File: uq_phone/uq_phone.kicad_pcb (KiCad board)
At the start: 4 copper layers, 116.9 x 105 mm, 164 parts, among them J1 USB4105-GF-A, J10 SJ-3551B-MSMT-TR-67, J11 Conn_01x02, J2 S3B-PH-SM4-TB_LF__SN_, J3 20279-001E-03, J4 20279-001E-03, J6 Conn_ARM_SWD_TagConnect_TC2030, J7 Conn_01x02, J8 KP15B-6S-SF_800_, J9 541324562, M1 VCDM0834B004L, Q1 MMBT3904LP-7, Q2 MMBT3904LP-7, U1 MCP73871-2CCI_ML, U10 TPD3F303DQDR, U11 TPD8F003DQDR, U12 MCP1664T-E/OT, U13 TS3A5018RSVR, U14 NAU88C22YG, U2 TPS62162DSGR, U3 BQ27441DRZR-G1A, U4 RC7620_1104625, U5 TXB0108RGYR, U6 TXB0108RGYR, U7 STM32H730VBTx, U8 LSM6DSVTR, U9 DRV2603RUNR

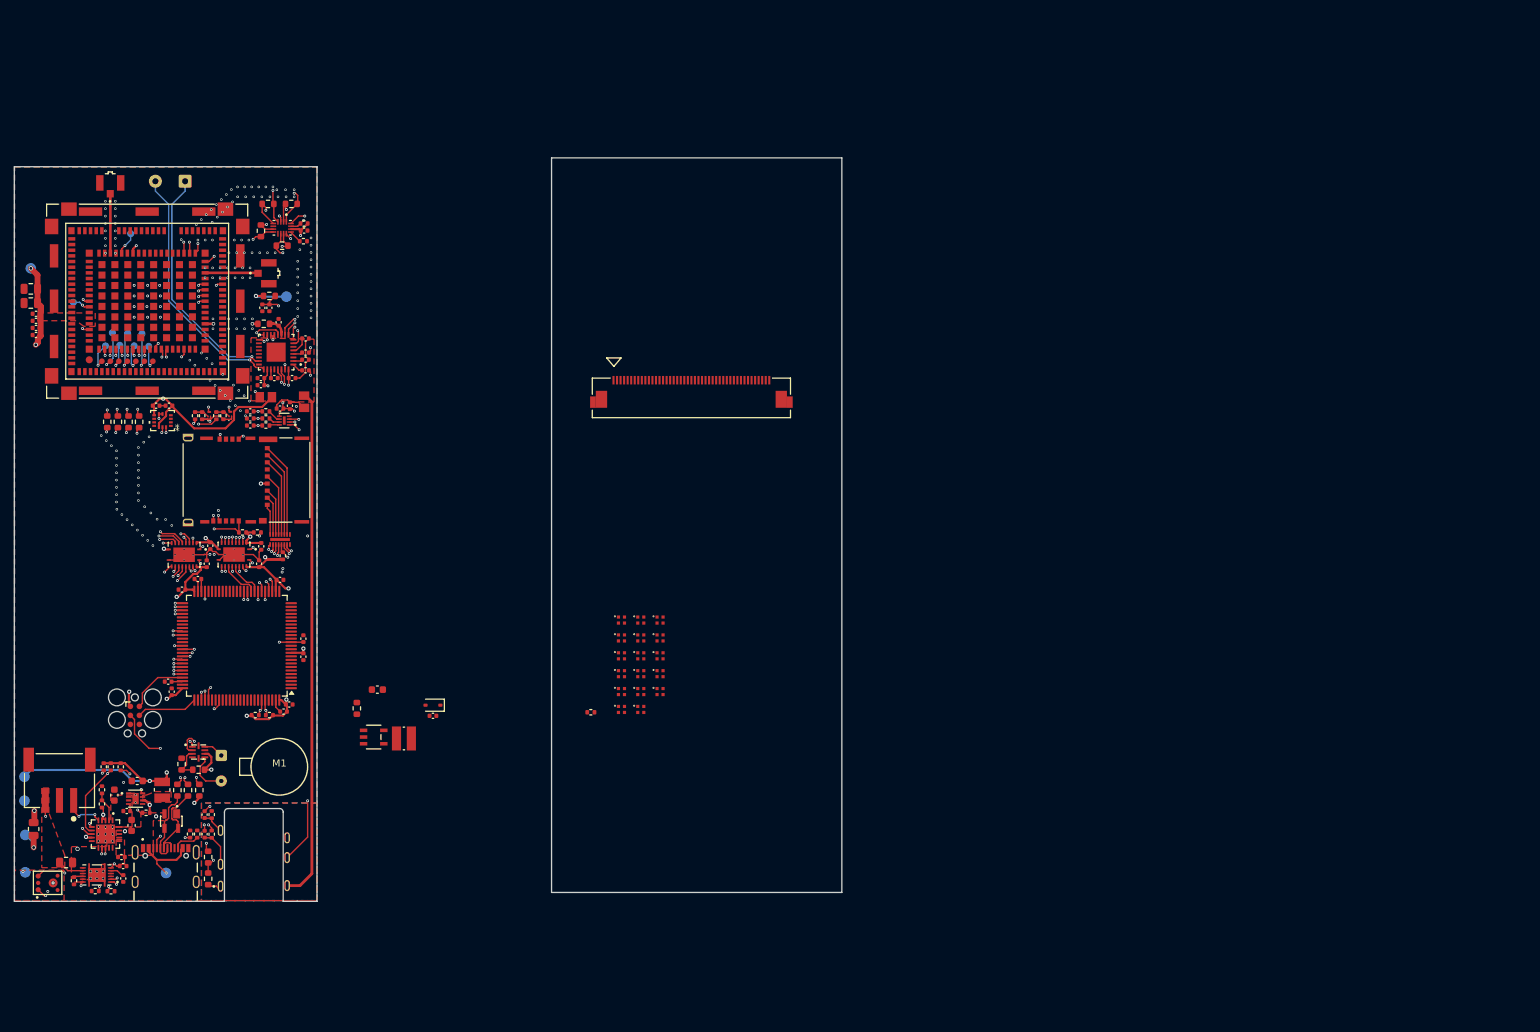
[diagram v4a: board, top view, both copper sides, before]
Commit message: Update pcb and remove Stm32 profile
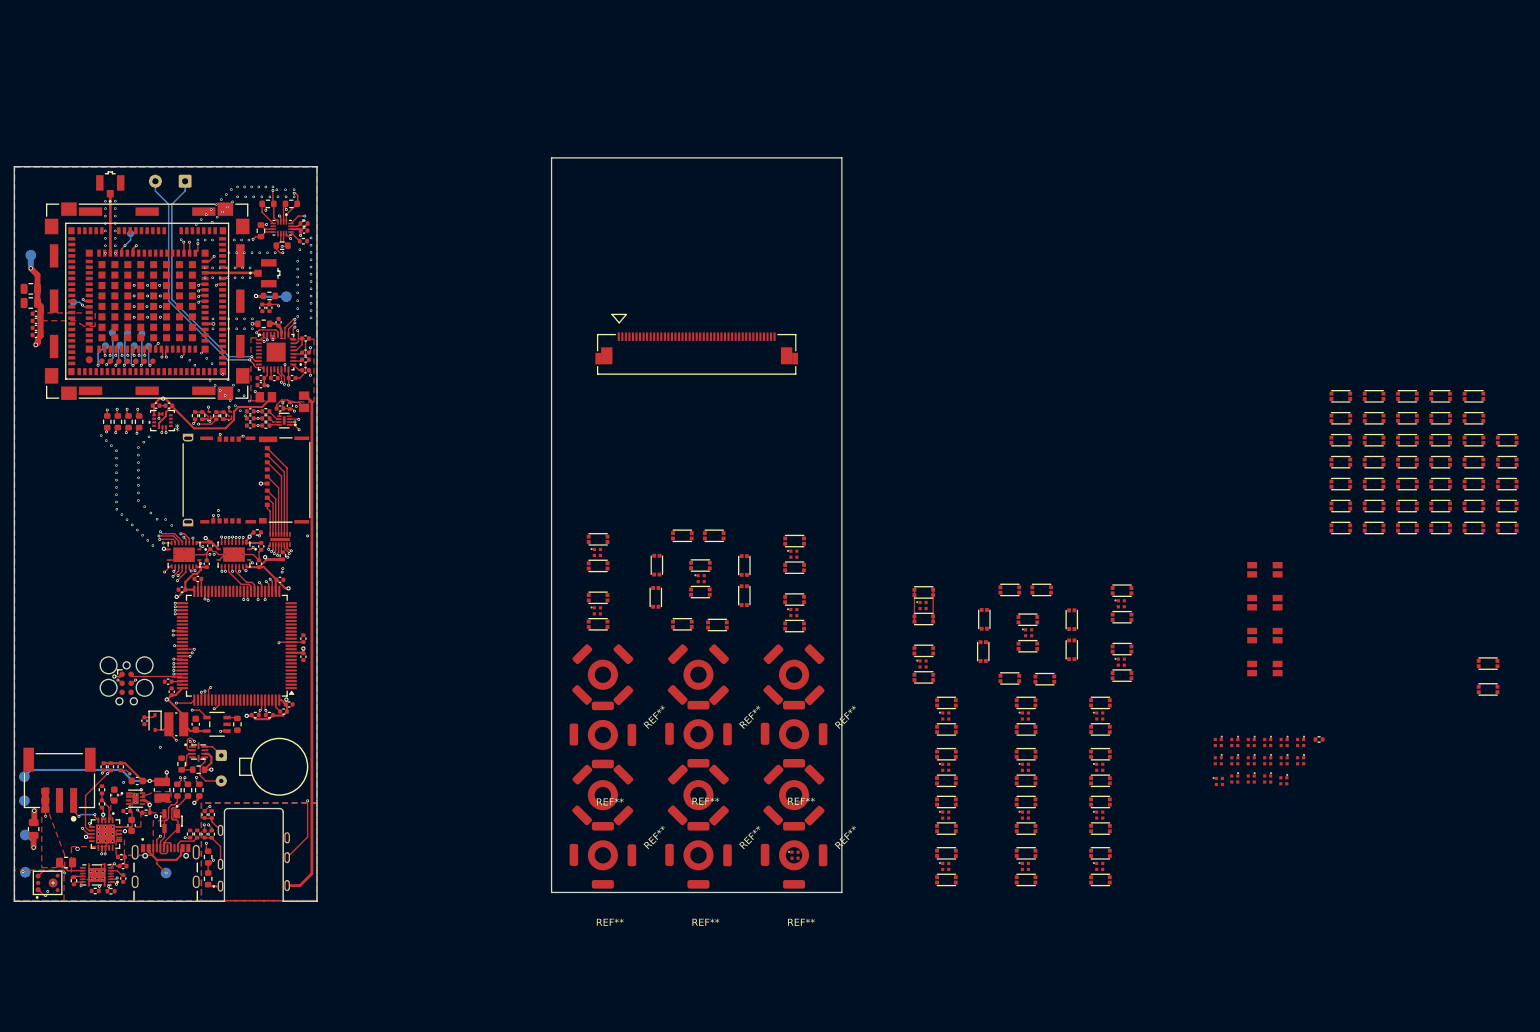
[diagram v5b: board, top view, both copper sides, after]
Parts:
- removed the LED13 at (118.2, 131.8)
- removed R23: 10k, Resistor_SMD:R_0402_1005Metric
- added LED13: XL-1010RGBC, custom_footprints:XL-1010RGBC-WS2812B, F.Cu at (137.1, 131.7)
- added LED13: XL-1010RGBC, custom_footprints:XL-1010RGBC-WS2812B, F.Cu at (169.8, 167.5)
- added LED13: XL-1010RGBC, custom_footprints:XL-1010RGBC-WS2812B, F.Cu at (180.2, 146.2)
- added LED13: XL-1010RGBC, custom_footprints:XL-1010RGBC-WS2812B, F.Cu at (137.1, 123.4)
- added LED13: XL-1010RGBC, custom_footprints:XL-1010RGBC-WS2812B, F.Cu at (155.3, 130.7)
- added LED13: XL-1010RGBC, custom_footprints:XL-1010RGBC-WS2812B, F.Cu at (158.5, 167.5)
- added LED13: XL-1010RGBC, custom_footprints:XL-1010RGBC-WS2812B, F.Cu at (180.2, 153.5)
- added LED13: XL-1010RGBC, custom_footprints:XL-1010RGBC-WS2812B, F.Cu at (124.0, 126.8)
- added LED13: XL-1010RGBC, custom_footprints:XL-1010RGBC-WS2812B, F.Cu at (180.2, 167.5)
- added LED13: XL-1010RGBC, custom_footprints:XL-1010RGBC-WS2812B, F.Cu at (170.2, 134.5)
- added LED13: XL-1010RGBC, custom_footprints:XL-1010RGBC-WS2812B, F.Cu at (183.3, 138.7)
- added LED13: XL-1010RGBC, custom_footprints:XL-1010RGBC-WS2812B, F.Cu at (158.5, 160.2)
- added LED13: XL-1010RGBC, custom_footprints:XL-1010RGBC-WS2812B, F.Cu at (137.2, 165.9)
- added LED13: XL-1010RGBC, custom_footprints:XL-1010RGBC-WS2812B, F.Cu at (109.3, 123.2)
- added LED13: XL-1010RGBC, custom_footprints:XL-1010RGBC-WS2812B, F.Cu at (197.2, 155.5)
- added LED13: XL-1010RGBC, custom_footprints:XL-1010RGBC-WS2812B, F.Cu at (155.3, 138.9)
- added LED13: XL-1010RGBC, custom_footprints:XL-1010RGBC-WS2812B, F.Cu at (169.8, 160.2)
- added LED13: XL-1010RGBC, custom_footprints:XL-1010RGBC-WS2812B, F.Cu at (183.3, 130.4)
- added LED13: XL-1010RGBC, custom_footprints:XL-1010RGBC-WS2812B, F.Cu at (169.8, 153.5)
- added LED13: XL-1010RGBC, custom_footprints:XL-1010RGBC-WS2812B, F.Cu at (158.5, 153.5)
- added LED13: XL-1010RGBC, custom_footprints:XL-1010RGBC-WS2812B, F.Cu at (169.8, 146.2)
- added LED13: XL-1010RGBC, custom_footprints:XL-1010RGBC-WS2812B, F.Cu at (109.3, 131.4)
- added LED13: XL-1010RGBC, custom_footprints:XL-1010RGBC-WS2812B, F.Cu at (180.2, 160.2)
- added LED13: XL-1010RGBC, custom_footprints:XL-1010RGBC-WS2812B, F.Cu at (158.5, 146.2)
- added REF**: 8.5mmSnaptron, custom_footprints:8.5mmSnaptron, F.Cu at (110.5, 157.0)
- added REF**: 8.5mmSnaptron, custom_footprints:8.5mmSnaptron, F.Cu at (124.0, 165.5)
- added REF**: 8.5mmSnaptron, custom_footprints:8.5mmSnaptron, F.Cu at (137.5, 140.0)
- added REF**: 8.5mmSnaptron, custom_footprints:8.5mmSnaptron, F.Cu at (137.5, 165.5)
- added REF**: 8.5mmSnaptron, custom_footprints:8.5mmSnaptron, F.Cu at (124.0, 157.0)
- added REF**: 8.5mmSnaptron, custom_footprints:8.5mmSnaptron, F.Cu at (110.5, 148.5)
- added REF**: 8.5mmSnaptron, custom_footprints:8.5mmSnaptron, F.Cu at (124.0, 148.4)
- added REF**: 8.5mmSnaptron, custom_footprints:8.5mmSnaptron, F.Cu at (124.0, 140.0)
- added REF**: 8.5mmSnaptron, custom_footprints:8.5mmSnaptron, F.Cu at (110.5, 140.0)
- added REF**: 8.5mmSnaptron, custom_footprints:8.5mmSnaptron, F.Cu at (137.5, 148.4)
- added REF**: 8.5mmSnaptron, custom_footprints:8.5mmSnaptron, F.Cu at (110.5, 165.5)
- added REF**: 8.5mmSnaptron, custom_footprints:8.5mmSnaptron, F.Cu at (137.5, 157.0)
- added SW1: SKTAAAE010, custom_footprints:SKTAAAE010, F.Cu at (213.4, 100.3)
- added SW10: SKTAAAE010, custom_footprints:SKTAAAE010, F.Cu at (218.1, 106.5)
- added SW11: SKTAAAE010, custom_footprints:SKTAAAE010, F.Cu at (218.1, 109.6)
- added SW12: SKTAAAE010, custom_footprints:SKTAAAE010, F.Cu at (218.1, 112.7)
- added SW13: SKTAAAE010, custom_footprints:SKTAAAE010, F.Cu at (218.1, 115.8)
- added SW14: SKTAAAE010, custom_footprints:SKTAAAE010, F.Cu at (218.1, 118.9)
- added SW15: SKTAAAE010, custom_footprints:SKTAAAE010, F.Cu at (222.8, 100.3)
- added SW16: SKTAAAE010, custom_footprints:SKTAAAE010, F.Cu at (222.8, 103.4)
- added SW17: SKTAAAE010, custom_footprints:SKTAAAE010, F.Cu at (222.8, 106.5)
- added SW18: SKTAAAE010, custom_footprints:SKTAAAE010, F.Cu at (222.8, 109.6)
- added SW19: SKTAAAE010, custom_footprints:SKTAAAE010, F.Cu at (222.8, 112.7)
- added SW2: SKTAAAE010, custom_footprints:SKTAAAE010, F.Cu at (213.4, 103.4)
- added SW20: SKTAAAE010, custom_footprints:SKTAAAE010, F.Cu at (222.8, 115.8)
- added SW21: SKTAAAE010, custom_footprints:SKTAAAE010, F.Cu at (222.8, 118.9)
- added SW22: SKTAAAE010, custom_footprints:SKTAAAE010, F.Cu at (227.5, 100.3)
- added SW23: SKTAAAE010, custom_footprints:SKTAAAE010, F.Cu at (227.5, 103.4)
- added SW24: SKTAAAE010, custom_footprints:SKTAAAE010, F.Cu at (227.5, 106.5)
- added SW25: SKTAAAE010, custom_footprints:SKTAAAE010, F.Cu at (227.5, 109.6)
- added SW26: SKTAAAE010, custom_footprints:SKTAAAE010, F.Cu at (227.5, 112.7)
- added SW27: SKTAAAE010, custom_footprints:SKTAAAE010, F.Cu at (227.5, 115.8)
- added SW28: SKTAAAE010, custom_footprints:SKTAAAE010, F.Cu at (227.5, 118.9)
- added SW29: SKTAAAE010, custom_footprints:SKTAAAE010, F.Cu at (232.2, 100.3)
- added SW3: SKTAAAE010, custom_footprints:SKTAAAE010, F.Cu at (213.4, 106.5)
- added SW30: SKTAAAE010, custom_footprints:SKTAAAE010, F.Cu at (232.2, 103.4)
- added SW31: SKTAAAE010, custom_footprints:SKTAAAE010, F.Cu at (232.2, 106.5)
- added SW32: SKTAAAE010, custom_footprints:SKTAAAE010, F.Cu at (232.2, 109.6)
- added SW33: SKTAAAE010, custom_footprints:SKTAAAE010, F.Cu at (232.2, 112.7)
- added SW34: SKTAAAE010, custom_footprints:SKTAAAE010, F.Cu at (232.2, 115.8)
- added SW35: SKTAAAE010, custom_footprints:SKTAAAE010, F.Cu at (232.2, 118.9)
- added SW36: SKTAAAE010, custom_footprints:SKTAAAE010, F.Cu at (174.2, 141.0)
- added SW36: SKTAAAE010, custom_footprints:SKTAAAE010, F.Cu at (136.2, 132.8)
- added SW36: SKTAAAE010, custom_footprints:SKTAAAE010, F.Cu at (169.3, 140.9)
- added SW36: SKTAAAE010, custom_footprints:SKTAAAE010, F.Cu at (179.4, 157.6)
- added SW36: SKTAAAE010, custom_footprints:SKTAAAE010, F.Cu at (136.2, 129.0)
- added SW36: SKTAAAE010, custom_footprints:SKTAAAE010, F.Cu at (136.2, 124.5)
- added SW36: SKTAAAE010, custom_footprints:SKTAAAE010, F.Cu at (108.5, 132.5)
- added SW36: SKTAAAE010, custom_footprints:SKTAAAE010, F.Cu at (128.0, 133.3)
- added SW36: SKTAAAE010, custom_footprints:SKTAAAE010, F.Cu at (179.4, 161.3)
- added SW36: SKTAAAE010, custom_footprints:SKTAAAE010, F.Cu at (179.4, 164.8)
- added SW36: SKTAAAE010, custom_footprints:SKTAAAE010, F.Cu at (176.3, 133.6)
- added SW36: SKTAAAE010, custom_footprints:SKTAAAE010, F.Cu at (164.0, 133.5)
- added SW36: SKTAAAE010, custom_footprints:SKTAAAE010, F.Cu at (123.0, 128.0)
- added SW36: SKTAAAE010, custom_footprints:SKTAAAE010, F.Cu at (169.2, 135.6)
- added SW36: SKTAAAE010, custom_footprints:SKTAAAE010, F.Cu at (108.5, 120.5)
- added SW36: SKTAAAE010, custom_footprints:SKTAAAE010, F.Cu at (157.7, 154.6)
- added SW36: SKTAAAE010, custom_footprints:SKTAAAE010, F.Cu at (179.4, 143.6)
- added SW36: SKTAAAE010, custom_footprints:SKTAAAE010, F.Cu at (117.8, 125.8)
- added SW36: SKTAAAE010, custom_footprints:SKTAAAE010, F.Cu at (168.9, 154.6)
- added SW36: SKTAAAE010, custom_footprints:SKTAAAE010, F.Cu at (169.2, 131.8)
- added SW36: SKTAAAE010, custom_footprints:SKTAAAE010, F.Cu at (123.0, 133.2)
- added SW36: SKTAAAE010, custom_footprints:SKTAAAE010, F.Cu at (157.7, 143.6)
- added SW36: SKTAAAE010, custom_footprints:SKTAAAE010, F.Cu at (154.5, 131.8)
- added SW36: SKTAAAE010, custom_footprints:SKTAAAE010, F.Cu at (179.4, 147.3)
- added SW36: SKTAAAE010, custom_footprints:SKTAAAE010, F.Cu at (154.5, 136.2)
- added SW36: SKTAAAE010, custom_footprints:SKTAAAE010, F.Cu at (154.5, 128.0)
- added SW36: SKTAAAE010, custom_footprints:SKTAAAE010, F.Cu at (157.7, 147.3)
- added SW36: SKTAAAE010, custom_footprints:SKTAAAE010, F.Cu at (108.5, 128.8)
- added SW36: SKTAAAE010, custom_footprints:SKTAAAE010, F.Cu at (127.5, 120.8)
- added SW36: SKTAAAE010, custom_footprints:SKTAAAE010, F.Cu at (123.0, 120.8)
- added SW36: SKTAAAE010, custom_footprints:SKTAAAE010, F.Cu at (168.9, 161.3)
- added SW36: SKTAAAE010, custom_footprints:SKTAAAE010, F.Cu at (182.5, 136.0)
- added SW36: SKTAAAE010, custom_footprints:SKTAAAE010, F.Cu at (234.2, 138.1)
- added SW36: SKTAAAE010, custom_footprints:SKTAAAE010, F.Cu at (157.7, 168.6)
- added SW36: SKTAAAE010, custom_footprints:SKTAAAE010, F.Cu at (157.7, 164.8)
- added SW36: SKTAAAE010, custom_footprints:SKTAAAE010, F.Cu at (157.7, 150.8)
- added SW36: SKTAAAE010, custom_footprints:SKTAAAE010, F.Cu at (108.5, 124.2)
- added SW36: SKTAAAE010, custom_footprints:SKTAAAE010, F.Cu at (179.4, 150.8)
- added SW36: SKTAAAE010, custom_footprints:SKTAAAE010, F.Cu at (136.2, 120.8)
- added SW36: SKTAAAE010, custom_footprints:SKTAAAE010, F.Cu at (157.7, 157.6)
- added SW36: SKTAAAE010, custom_footprints:SKTAAAE010, F.Cu at (179.4, 168.6)
- added SW36: SKTAAAE010, custom_footprints:SKTAAAE010, F.Cu at (130.1, 125.9)
- added SW36: SKTAAAE010, custom_footprints:SKTAAAE010, F.Cu at (168.9, 150.8)
- added SW36: SKTAAAE010, custom_footprints:SKTAAAE010, F.Cu at (168.9, 164.8)
- added SW36: SKTAAAE010, custom_footprints:SKTAAAE010, F.Cu at (168.9, 147.3)
- added SW36: SKTAAAE010, custom_footprints:SKTAAAE010, F.Cu at (163.8, 138.1)
- added SW36: SKTAAAE010, custom_footprints:SKTAAAE010, F.Cu at (169.3, 128.4)
- added SW36: SKTAAAE010, custom_footprints:SKTAAAE010, F.Cu at (179.4, 154.6)
- added SW36: SKTAAAE010, custom_footprints:SKTAAAE010, F.Cu at (130.1, 130.2)
- added SW36: SKTAAAE010, custom_footprints:SKTAAAE010, F.Cu at (123.0, 124.2)
- added SW36: SKTAAAE010, custom_footprints:SKTAAAE010, F.Cu at (182.5, 127.8)
- added SW36: SKTAAAE010, custom_footprints:SKTAAAE010, F.Cu at (176.3, 137.8)
- added SW36: SKTAAAE010, custom_footprints:SKTAAAE010, F.Cu at (168.9, 157.6)
- added SW36: SKTAAAE010, custom_footprints:SKTAAAE010, F.Cu at (154.5, 140.0)
- added SW36: SKTAAAE010, custom_footprints:SKTAAAE010, F.Cu at (157.7, 161.3)
- added SW36: SKTAAAE010, custom_footprints:SKTAAAE010, F.Cu at (117.6, 130.4)
- added SW36: SKTAAAE010, custom_footprints:SKTAAAE010, F.Cu at (168.9, 143.6)
- added SW36: SKTAAAE010, custom_footprints:SKTAAAE010, F.Cu at (173.8, 128.4)
- added SW36: SKTAAAE010, custom_footprints:SKTAAAE010, F.Cu at (182.5, 131.5)
- added SW36: SKTAAAE010, custom_footprints:SKTAAAE010, F.Cu at (168.9, 168.6)
- added SW36: SKTAAAE010, custom_footprints:SKTAAAE010, F.Cu at (182.5, 139.8)
- added SW37: SKTAAAE010, custom_footprints:SKTAAAE010, F.Cu at (234.2, 141.7)
- added SW38: SKTAAAE010, custom_footprints:SKTAAAE010, F.Cu at (236.9, 106.5)
- added SW39: SKTAAAE010, custom_footprints:SKTAAAE010, F.Cu at (236.9, 109.6)
- added SW4: SKTAAAE010, custom_footprints:SKTAAAE010, F.Cu at (213.4, 109.6)
- added SW40: SKTAAAE010, custom_footprints:SKTAAAE010, F.Cu at (236.9, 112.7)
- added SW41: SKTAAAE010, custom_footprints:SKTAAAE010, F.Cu at (236.9, 115.8)
- added SW42: SKTAAAE010, custom_footprints:SKTAAAE010, F.Cu at (236.9, 118.9)
- added SW43: SKSCLCE010, custom_footprints:SKSCLCE010, F.Cu at (202.2, 125.8)
- added SW44: SKSCLCE010, custom_footprints:SKSCLCE010, F.Cu at (202.2, 130.5)
- added SW45: SKSCLCE010, custom_footprints:SKSCLCE010, F.Cu at (202.2, 135.1)
- added SW46: SKSCLCE010, custom_footprints:SKSCLCE010, F.Cu at (202.2, 139.8)
- added SW5: SKTAAAE010, custom_footprints:SKTAAAE010, F.Cu at (213.4, 112.7)
- added SW6: SKTAAAE010, custom_footprints:SKTAAAE010, F.Cu at (213.4, 115.8)
- added SW7: SKTAAAE010, custom_footprints:SKTAAAE010, F.Cu at (213.4, 118.9)
- added SW8: SKTAAAE010, custom_footprints:SKTAAAE010, F.Cu at (218.1, 100.3)
- added SW9: SKTAAAE010, custom_footprints:SKTAAAE010, F.Cu at (218.1, 103.4)
- moved R48 102.9 mm to (211.7, 149.1), turned to 0 degrees
- moved LED6 96.0 mm to (208.6, 149.2)
- moved LED5 93.9 mm to (206.3, 149.2)
- moved LED12 93.5 mm to (208.6, 151.7)
- moved LED4 91.8 mm to (204.0, 149.2)
- moved LED11 91.4 mm to (206.3, 151.7)
- moved LED3 89.8 mm to (201.7, 149.2)
- moved LED10 89.4 mm to (204.0, 151.7)
- moved LED17 89.0 mm to (206.2, 154.6)
- moved LED2 87.9 mm to (199.3, 149.2)
- moved LED9 87.5 mm to (201.7, 151.7)
- moved LED16 87.1 mm to (204.0, 154.3)
- moved LED1 86.1 mm to (197.0, 149.2)
- moved LED8 85.7 mm to (199.3, 151.7)
- moved LED15 85.3 mm to (201.7, 154.3)
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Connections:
- J8 pad D_T_2: SIM_DET -> unconnected-(J8-PadD_T_2)
- U4 pad 64: SIM_DET -> unconnected-(U4A-UIM1_SIMA_DET-Pad64)
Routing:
- net SIM_DET: track 45.8 -> 0.00 mm, vias 2 -> 0
- net DISP_BL: track 0.00 -> 20.2 mm, vias 0 -> 2
- net Net-(D2-A): track 0.00 -> 13.1 mm, vias 0 -> 2
- net +3.3V: track 227.3 -> 237.3 mm
- net (no net): track 0.00 -> 9.00 mm
- net RST: track 37.6 -> 42.0 mm, vias 2 -> 3
- net SWCLK: track 8.66 -> 11.9 mm, vias 0 -> 2
- net +VMOB: track 80.0 -> 81.8 mm
- net DISP_LEDA: track 0.00 -> 1.63 mm
- net DISP_LEDK: track 0.00 -> 1.50 mm
- net SWDIO: track 8.64 -> 7.49 mm
- net +1.8V: track 116.0 -> 114.9 mm
- net MOB_PWR: track 30.0 -> 29.4 mm
